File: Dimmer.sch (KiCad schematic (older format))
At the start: 62 parts, among them J1 220to12, J10 Detect_nullA, J11 220v_OUT, J12 Load_cntrlA, J13 ADC, J14 Conn_01x01, J15 Conn_01x01, J16 Conn_01x01, J17 Conn_01x01, J18 Conn_01x01, J19 Conn_01x01, J2 Prog, J22 SPI, J3 UART0, J4 Mode, J5 Load_cntrl, J6 Detect_null, J7 I2C, J8 ADC, J9 220v_IN, Q1 IRFP460APBF, Q2 IRFP460APBF, Q3 BC807, SW1 SW_Push, SW2 SW_Push, U2 ESP32-WROOM-32D, U3 L78L33_SO8, U4 TLP185, k1 Key, k2 Key, k3 Key, k4 Key, k5 Key, k6 Key, k7 Key

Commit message: Add files via upload
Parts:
- removed J10: Detect_nullA, Connector:FanPinHeader_1x03_P2.54mm_Vertical, symbol Connector_Generic:Conn_01x03
- removed J12: Load_cntrlA, Connector:FanPinHeader_1x03_P2.54mm_Vertical, symbol Connector_Generic:Conn_01x03
- removed J16, J17, J18, J19: Conn_01x01, Touch_pad:polz_razjem, symbol Connector_Generic:Conn_01x01
- removed J4: Mode, Connector_PinHeader_2.54mm:PinHeader_1x04_P2.54mm_Vertical_SMD_Pin1Left, symbol Connector_Generic:Conn_01x02
- removed J5: Load_cntrl, Connector:FanPinHeader_1x03_P2.54mm_Vertical, symbol Connector_Generic:Conn_01x03
- removed J6: Detect_null, Connector:FanPinHeader_1x03_P2.54mm_Vertical, symbol Connector_Generic:Conn_01x03
- removed k1: Key, Touch_pad:TestPoint_Pad_2.5x2.5sm, symbol Dimmer-rescue:Key-Touchpad-Dimmer-rescue
- added J10, J12, J5, J6: Pin, SMout:polz_razjem, symbol Connector_Generic:Conn_01x01
- added J16, J4: Conn_01x05, Connector_PinHeader_2.54mm:PinHeader_1x05_P2.54mm_Vertical, symbol Connector_Generic:Conn_01x05
- added J20: Rst, SMout:polz_razjem, symbol Connector_Generic:Conn_01x01
- added J23: Mode, SMout:2pins, symbol Connector_Generic:Conn_01x02
- C1, C8: footprint Capacitor_SMD:C_1210_3225Metric -> Capacitor_SMD:C_0402_1005Metric
- C11, C2: footprint Capacitor_SMD:C_1210_3225Metric -> Capacitor_SMD:C_0805_2012Metric
- J1: footprint Converter_ACDC:Converter_ACDC_MeanWell_IRM-02-xx_THT -> SMout:oblast_bp; symbol Dimmer-rescue:HEADER_2x2-w_connectors-Dimmer-rescue -> Dimmer-rescue:HEADER_2x2-w_connectors-Dimmer-rescue-Dimmer-rescue
- J11, J9: footprint Connector_Phoenix_MC_HighVoltage:PhoenixContact_MC_1,5_2-G-5.08_1x02_P5.08mm_Horizontal -> SMout:OUT_IN(1)
- J13, J8: footprint Touch_pad:polz_razjem -> SMout:polz_razjem
- J14, J15: value Conn_01x01 -> Pin; footprint Touch_pad:polz_razjem -> SMout:polz_razjem
- J2: footprint Connector_PinHeader_2.54mm:PinHeader_1x02_P2.54mm_Vertical_SMD_Pin1Left -> SMout:2pins
- J22: footprint Connector_PinHeader_2.54mm:PinHeader_1x04_P2.54mm_Vertical_SMD_Pin1Right -> Connector_PinHeader_2.54mm:PinHeader_1x03_P2.54mm_Vertical_SMD_Pin1Right
- R10: footprint Resistor_SMD:R_0603_1608Metric -> Resistor_SMD:R_1206_3216Metric
- R13, R2, R9: footprint Resistor_SMD:R_0603_1608Metric -> Resistor_SMD:R_0805_2012Metric
- R7: footprint Resistor_SMD:R_0603_1608Metric -> Resistor_SMD:R_2512_6332Metric
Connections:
- net GPIO26 is gone; now on net cntrl: U2.11 (IO26)
- net +3V3: now also J16.1 (Pin_1), J4.1 (Pin_1)
- net GND: now also J16.5 (Pin_5), J4.5 (Pin_5)
- net Mode: now also J23.1 (Pin_1)
- net cntrl: now also J16.2 (Pin_2); no longer D7.3 (IN+)
- net at R2.2, SW1.2, U2.3 (EN): now also J20.1 (Pin_1)
- net at SW2.2: now also J23.2 (Pin_2)
- net at U2.17 (SHD/SD2): now also J6.1 (Pin_1)
- net at U2.18 (SWP/SD3): now also J10.1 (Pin_1)
- net at U2.19 (SCS/CMD): now also J15.1 (Pin_1)
- net at U2.20 (SCK/CLK): now also J12.1 (Pin_1)
- net at U2.22 (SDI/SD1): now also J5.1 (Pin_1); no longer J15.1 (Pin_1)
- net Detect_null: now reaches U4.6
- net Detect_null: now also J4.4 (Pin_4)
- net at R9.2, TH1.1: now also J4.3 (Pin_3)
- net GPIO17 renamed null
- net null: now also J16.4 (Pin_4)
- net GPIO32 renamed termo_bp
- net termo_bp: now also J16.3 (Pin_3)
- net GPIO35 renamed photo
- new net Load_cntrl: D7.3 (IN+), J4.2 (Pin_2)
- no-connect marks 0 -> 1
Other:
- moved on the sheet: J22, SW2

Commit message: Add files via upload
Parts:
- removed TH1, TH2: Thermistor_NTC, Resistor_SMD:R_1206_3216Metric_Pad1.30x1.75mm_HandSolder, symbol Device:Thermistor_NTC
- added J17: I2C, Connector_PinSocket_2.54mm:PinSocket_1x03_P2.54mm_Horizontal, symbol Connector_Generic:Conn_01x03
- added U1: LM75B, SMout:Diodes_SO-8, symbol Sensor_Temperature:LM75B
- J7: footprint Connector_PinHeader_2.54mm:PinHeader_1x04_P2.54mm_Horizontal -> Connector_PinSocket_2.54mm:PinSocket_1x03_P2.54mm_Horizontal
- R13, R9: footprint Resistor_SMD:R_0805_2012Metric -> Resistor_SMD:R_0603_1608Metric
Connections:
- net +3V3: now also U1.8 (+Vs)
- net GND: now also J17.3 (Pin_3), U1.4 (GND), U1.5 (A2), U1.6 (A1), U1.7 (A0)
- net O.S.: now reaches U2.26 (IO4)
- net O.S.: now also J16.3 (Pin_3)
- net at U2.6 (IO34): no longer R13.2
- net at J4.3 (Pin_3): now also U1.3 (O.S.); no longer R9.2
- net termo_bp: no longer names the net of U2.10 (IO25)
- net termo_bp: no longer J16.3 (Pin_3)
- new net SCL: J17.2 (Pin_2), R13.2, U1.2 (SCL)
- new net SDA: J17.1 (Pin_1), R9.2, U1.1 (SDA)
- no-connect marks 1 -> 2
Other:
- moved on the sheet: C11, C8, J4, U3

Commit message: Add files via upload
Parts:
- C1, C8: footprint Capacitor_SMD:C_0402_1005Metric -> Capacitor_SMD:C_0805_2012Metric
- D5, D6: footprint LED_THT:LED_D3.0mm_Clear -> LED_SMD:LED_0805_2012Metric
- J17: footprint Connector_PinSocket_2.54mm:PinSocket_1x03_P2.54mm_Horizontal -> Connector_PinSocket_2.54mm:PinSocket_1x03_P2.54mm_Vertical
- J22: footprint Connector_PinHeader_2.54mm:PinHeader_1x03_P2.54mm_Vertical_SMD_Pin1Right -> Connector_PinHeader_2.54mm:PinHeader_1x04_P2.54mm_Vertical
- J3: footprint Connector_PinHeader_2.54mm:PinHeader_1x04_P2.54mm_Horizontal -> SMout:4pins
- J7: footprint Connector_PinSocket_2.54mm:PinSocket_1x03_P2.54mm_Horizontal -> Connector_PinHeader_2.54mm:PinHeader_1x03_P2.54mm_Horizontal
- R3: footprint OptoDevice:R_LDR_5.1x4.3mm_P3.4mm_Vertical -> SMout:R_LDR_5.1x4.3mm_P3.4mm_Vertical
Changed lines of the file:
@@
 F 0 "C8" H 5218 4031 50  0000 L CNN
 F 1 "0.1mk" H 5218 3940 50  0000 L CNN
-F 2 "Capacitor_SMD:C_0402_1005Metric" H 5040 3985 50  0001 C CNN
+F 2 "Capacitor_SMD:C_0805_2012Metric" H 5040 3985 50  0001 C CNN
 F 3 "~" H 5040 3985 50  0001 C CNN
 	1    5040 3985
@@
 F 0 "J7" H 9130 4642 50  0000 L CNN
 F 1 "I2C" H 9130 4551 50  0000 L CNN
-F 2 "Connector_PinSocket_2.54mm:PinSocket_1x03_P2.54mm_Horizontal" H 9050 4600 50  0001 C CNN
+F 2 "Connector_PinHeader_2.54mm:PinHeader_1x03_P2.54mm_Horizontal" H 9050 4600 50  0001 C CNN
 F 3 "~" H 9050 4600 50  0001 C CNN
 	1    9050 4600
@@
 $EndComp
 $Comp
-L Connector_Generic:Conn_01x02 J2
-U 1 1 60C48D5A
-P 8800 2750
-F 0 "J2" H 8880 2742 50  0000 L CNN
-F 1 "Prog" H 8880 2651 50  0000 L CNN
-F 2 "SMout:2pins" H 8800 2750 50  0001 C CNN
-F 3 "~" H 8800 2750 50  0001 C CNN
-	1    8800 2750
-	1    0    0    -1
-$EndComp
-$Comp
 L Connector_Generic:Conn_01x04 J3
 U 1 1 60C3C307
@@
 F 0 "J3" H 9280 3292 50  0000 L CNN
 F 1 "UART0" H 9280 3201 50  0000 L CNN
-F 2 "Connector_PinHeader_2.54mm:PinHeader_1x04_P2.54mm_Horizontal" H 9200 3300 50  0001 C CNN
+F 2 "SMout:4pins" H 9200 3300 50  0001 C CNN
 F 3 "~" H 9200 3300 50  0001 C CNN
 	1    9200 3300
@@
 F 0 "C1" H 1928 2996 50  0000 L CNN
 F 1 "0.01mk" H 1928 2905 50  0000 L CNN
-F 2 "Capacitor_SMD:C_0402_1005Metric" H 1750 2950 50  0001 C CNN
+F 2 "Capacitor_SMD:C_0805_2012Metric" H 1750 2950 50  0001 C CNN
 F 3 "~" H 1750 2950 50  0001 C CNN
 	1    1750 2950
@@
 F 0 "R3" H 9370 5946 50  0000 L CNN
 F 1 "GL5528" H 9370 5855 50  0000 L CNN
-F 2 "OptoDevice:R_LDR_5.1x4.3mm_P3.4mm_Vertical" V 9350 5650 50  0001 L CNN
+F 2 "SMout:R_LDR_5.1x4.3mm_P3.4mm_Vertical" V 9350 5650 50  0001 L CNN
 F 3 "~" H 9300 5850 50  0001 C CNN
 	1    9300 5900
@@
 F 0 "D5" V 9889 5432 50  0000 R CNN
 F 1 "BLUE" V 9798 5432 50  0000 R CNN
-F 2 "LED_THT:LED_D3.0mm_Clear" H 9850 5550 50  0001 C CNN
+F 2 "LED_SMD:LED_0805_2012Metric" H 9850 5550 50  0001 C CNN
 F 3 "~" H 9850 5550 50  0001 C CNN
 	1    9850 5550
@@
 F 0 "D6" V 10289 5432 50  0000 R CNN
 F 1 "RED" V 10198 5432 50  0000 R CNN
-F 2 "LED_THT:LED_D3.0mm_Clear" H 10250 5550 50  0001 C CNN
+F 2 "LED_SMD:LED_0805_2012Metric" H 10250 5550 50  0001 C CNN
 F 3 "~" H 10250 5550 50  0001 C CNN
 	1    10250 5550
@@
 F 0 "J22" H 9135 4217 50  0000 L CNN
 F 1 "SPI" H 9135 4126 50  0000 L CNN
-F 2 "Connector_PinHeader_2.54mm:PinHeader_1x03_P2.54mm_Vertical_SMD_Pin1Right" H 9055 4225 50  0001 C CNN
+F 2 "Connector_PinHeader_2.54mm:PinHeader_1x04_P2.54mm_Vertical" H 9055 4225 50  0001 C CNN
 F 3 "~" H 9055 4225 50  0001 C CNN
 	1    9055 4225
@@
 F 0 "J17" H 3010 4862 50  0000 L CNN
 F 1 "I2C" H 3010 4771 50  0000 L CNN
-F 2 "Connector_PinSocket_2.54mm:PinSocket_1x03_P2.54mm_Horizontal" H 2930 4820 50  0001 C CNN
+F 2 "Connector_PinSocket_2.54mm:PinSocket_1x03_P2.54mm_Vertical" H 2930 4820 50  0001 C CNN
 F 3 "~" H 2930 4820 50  0001 C CNN
 	1    2930 4820
@@
 	1    0    0    -1
 $EndComp
+$Comp
+L Connector_Generic:Conn_01x02 J2
+U 1 1 60C48D5A
+P 8800 2750
+F 0 "J2" H 8880 2742 50  0000 L CNN
+F 1 "Prog" H 8880 2651 50  0000 L CNN
+F 2 "SMout:2pins" H 8800 2750 50  0001 C CNN
+F 3 "~" H 8800 2750 50  0001 C CNN
+	1    8800 2750
+	1    0    0    -1
+$EndComp

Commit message: New regulator, buttons
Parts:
- removed J17: I2C, Connector_PinSocket_2.54mm:PinSocket_1x03_P2.54mm_Vertical, symbol Connector_Generic:Conn_01x03
- removed J23: Mode, SMout:2pins, symbol Connector_Generic:Conn_01x02
- removed J7: I2C, Connector_PinHeader_2.54mm:PinHeader_1x03_P2.54mm_Horizontal, symbol Connector_Generic:Conn_01x03
- removed U3: L78L33_SO8, Package_SO:SOIC-8_3.9x4.9mm_P1.27mm, symbol Regulator_Linear:L78L33_SO8
- added U22: AMS1117-3.3, Package_TO_SOT_SMD:SOT-223-3_TabPin2, symbol Regulator_Linear:AMS1117-3.3
- C11: value 0.33mk -> 1uF
- C8: value 0.1mk -> 0.1uF
- J16, J4: value Conn_01x05 -> Conn_01x06; footprint Connector_PinHeader_2.54mm:PinHeader_1x05_P2.54mm_Vertical -> Connector_PinHeader_2.54mm:PinHeader_1x06_P2.54mm_Vertical; symbol Connector_Generic:Conn_01x05 -> Connector_Generic:Conn_01x06
- Mode1: renamed from SW2; footprint Button_Switch_SMD:SW_DIP_SPSTx01_Slide_6.7x4.1mm_W6.73mm_P2.54mm_LowProfile_JPin -> Touch_pad:aLIEXPRESS_BUTTON_G71Y
- RST2: renamed from SW1; footprint Button_Switch_SMD:SW_DIP_SPSTx01_Slide_6.7x4.1mm_W6.73mm_P2.54mm_LowProfile_JPin -> Touch_pad:aLIEXPRESS_BUTTON_G71Y
- renumbered J12 to CLK1, J15 to CMD1, J20 to RST1, J14 to SD0, J5 to SD1, J6 to SD2, J10 to SD3, J13 to S_VN1, J8 to S_VP1
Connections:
- net +12V: now also U22.3 (VI)
- net +3V3: now also U22.2 (VO)
- net Detect_null: now also J4.3 (Pin_3); no longer J4.4 (Pin_4)
- net GND: now also J16.6 (Pin_6), J4.6 (Pin_6), RST2.2, U22.1 (GND); no longer J16.5 (Pin_5), J4.5 (Pin_5), RST2.1
- net Mode: now also Mode1.2
- net SCL: now also J16.4 (Pin_4), J4.4 (Pin_4), U2.36 (IO22)
- net SDA: now also J16.5 (Pin_5), J4.5 (Pin_5), U2.33 (IO21)
- net null: now also J16.3 (Pin_3); no longer J16.4 (Pin_4)
- net at R2.2, RST1.1 (Pin_1), U2.3 (EN): now also RST2.1; no longer RST2.2
- net at U1.3 (O.S.): no longer J4.3 (Pin_3)
- net O.S.: no longer names the net of U2.26 (IO4)
- net O.S.: no longer J16.3 (Pin_3)
- no-connect marks 2 -> 4
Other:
- moved on the sheet: RST2

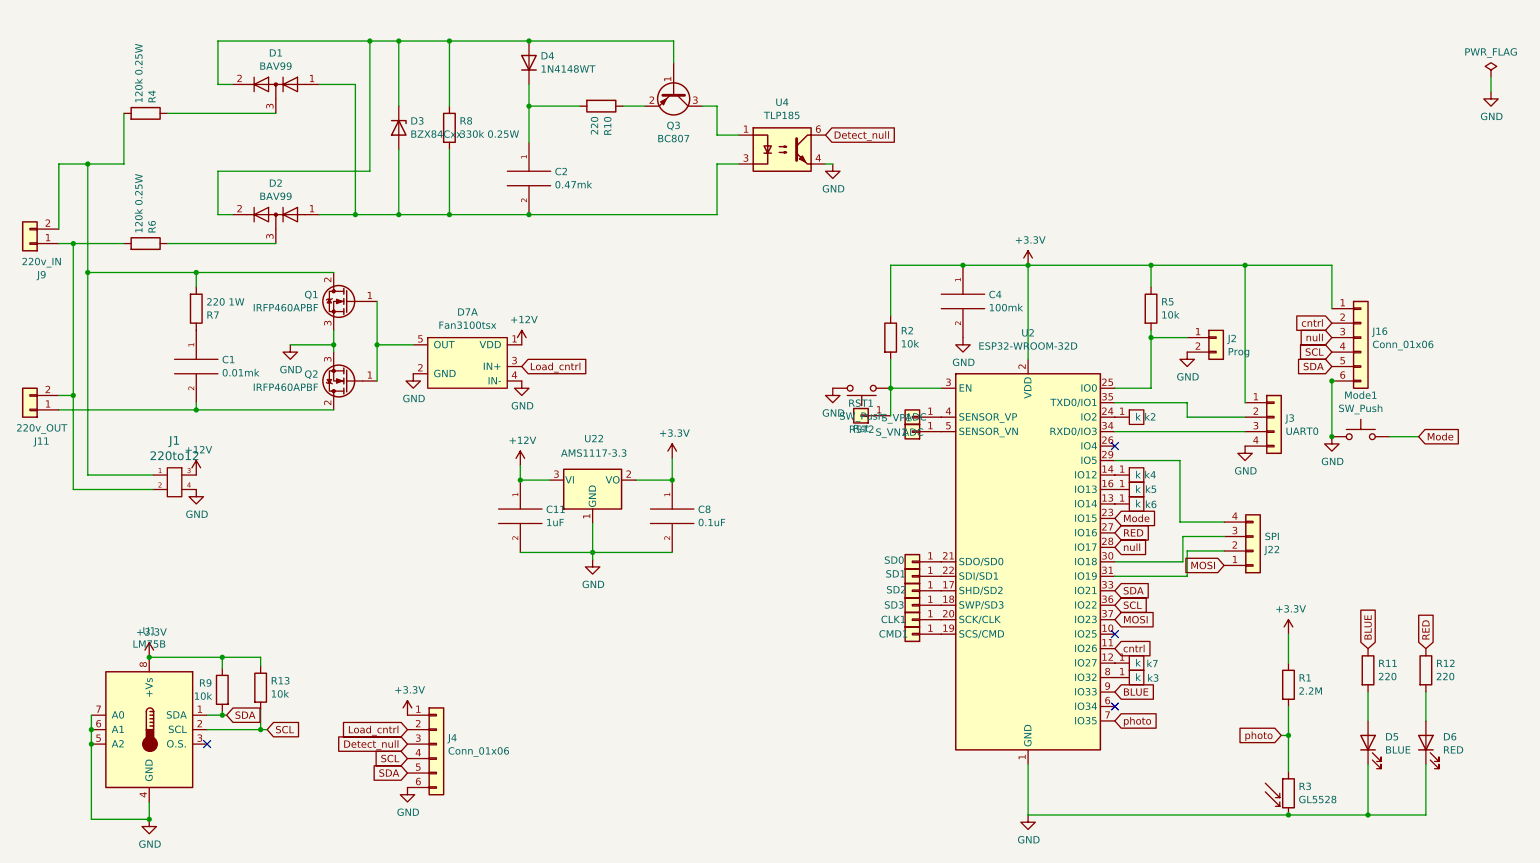
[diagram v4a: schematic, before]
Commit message: Заменены посадочные места, переразведена нижняя плата
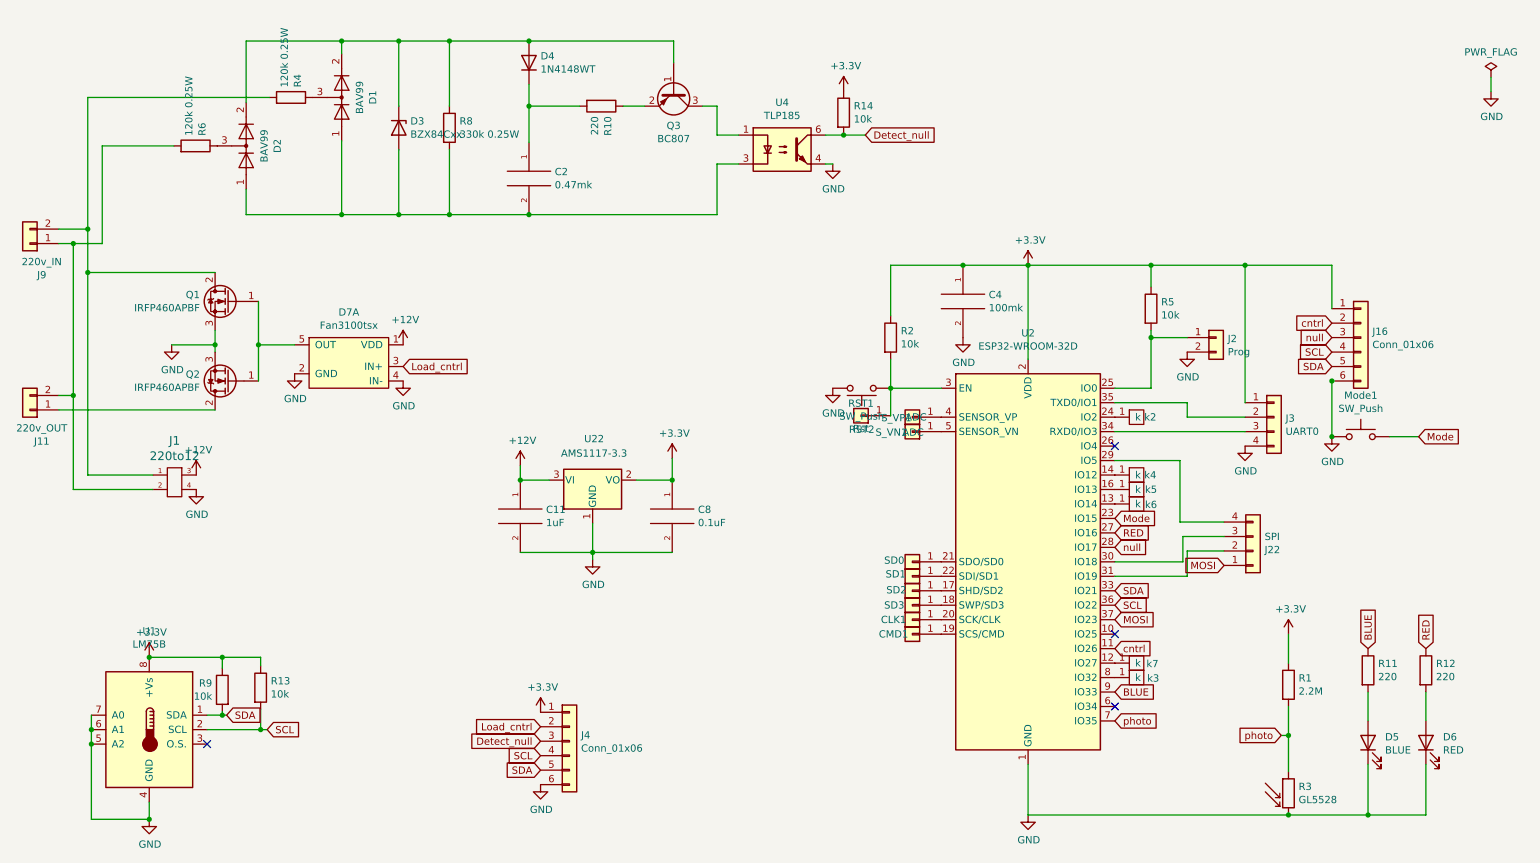
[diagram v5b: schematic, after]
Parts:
- removed C1: 0.01mk, Capacitor_SMD:C_0805_2012Metric, symbol pspice:C
- removed R7: 220 1W, Resistor_SMD:R_2512_6332Metric, symbol Device:R
- added R14: 10k, Resistor_SMD:R_0805_2012Metric, symbol Device:R
- C4: footprint Capacitor_SMD:C_1210_3225Metric -> Capacitor_SMD:C_0805_2012Metric
- D4: footprint Diode_SMD:D_SOD-523 -> Diode_SMD:D_SOD-123
- R1, R10, R11, R12: footprint Resistor_SMD:R_1206_3216Metric -> Resistor_SMD:R_0805_2012Metric
- R13, R4, R5, R6, R8, R9: footprint Resistor_SMD:R_0603_1608Metric -> Resistor_SMD:R_0805_2012Metric
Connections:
- net +3V3: now also R14.1
- net Detect_null: now also R14.2
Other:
- moved on the sheet: D1, D2, D7A, J4, Q1, Q2, R4, R6

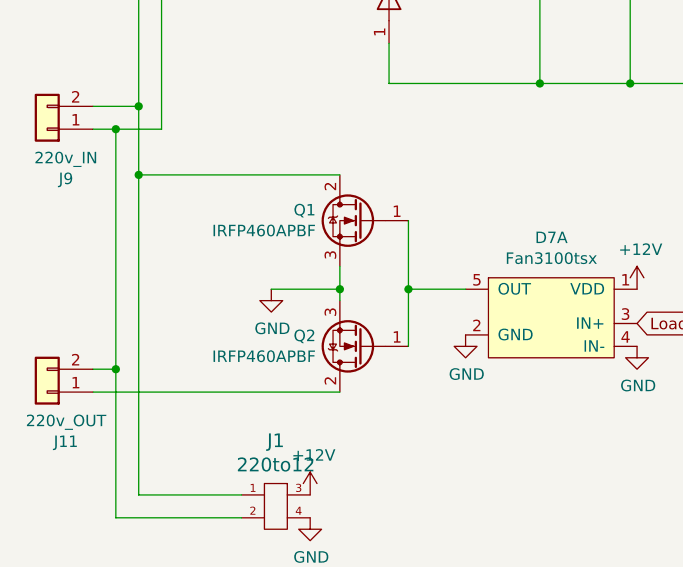
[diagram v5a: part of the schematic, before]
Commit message: Добавлены С1 и R7
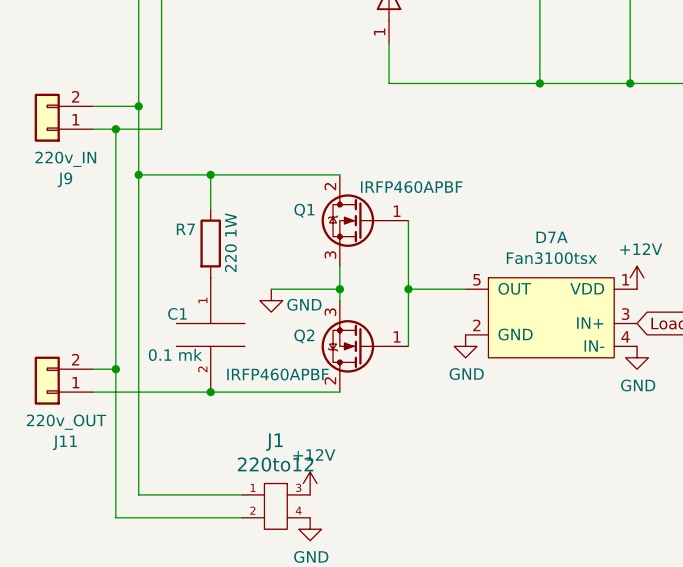
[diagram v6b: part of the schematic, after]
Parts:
- added C1: 0.1 mk, Capacitor_SMD:C_0805_2012Metric, symbol pspice:C
- added R7: 220 1W, Resistor_SMD:R_2512_6332Metric, symbol Device:R
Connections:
- net at J11.1 (Pin_1), Q2.2 (D): now also C1.2
- net at J1.1, J9.2 (Pin_2), Q1.2 (D)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: now also R7.1
- new net: C1.1, R7.2
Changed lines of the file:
@@
 P 1580 2800
 F 0 "#PWR0113" H 1580 2550 50  0001 C CNN
-F 1 "GND" H 1585 2627 50  0000 C CNN
+F 1 "GND" H 1725 2730 50  0000 C CNN
 F 2 "" H 1580 2800 50  0001 C CNN
 F 3 "" H 1580 2800 50  0001 C CNN
@@
 P 1980 3050
 F 0 "Q2" H 2185 3004 50  0000 L CNN
-F 1 "IRFP460APBF" H 2185 3095 50  0000 L CNN
+F 1 "IRFP460APBF" H 2125 3175 50  0000 L CNN
 F 2 "Package_TO_SOT_THT:TO-247-3_Horizontal_TabDown" H 1980 3050 50  0001 C CIN
 F 3 "https://www.wolfspeed.com/media/downloads/825/C3M0280090D.pdf" H 1980 3050 50  0001 L CNN
@@
 P 1980 2500
 F 0 "Q1" H 2185 2546 50  0000 L CNN
-F 1 "IRFP460APBF" H 2185 2455 50  0000 L CNN
+F 1 "IRFP460APBF" H 1540 2645 50  0000 L CNN
 F 2 "Package_TO_SOT_THT:TO-247-3_Horizontal_TabDown" H 1980 2500 50  0001 C CIN
 F 3 "https://www.wolfspeed.com/media/downloads/825/C3M0280090D.pdf" H 1980 2500 50  0001 L CNN
@@
 	1    0    0    -1
 $EndComp
+$Comp
+L pspice:C C1
+U 1 1 6168A513
+P 1315 3000
+F 0 "C1" H 1125 3090 50  0000 L CNN
+F 1 "0.1 mk" H 1040 2910 50  0000 L CNN
+F 2 "Capacitor_SMD:C_0805_2012Metric" H 1315 3000 50  0001 C CNN
+F 3 "~" H 1315 3000 50  0001 C CNN
+	1    1315 3000
+	1    0    0    -1
+$EndComp
+$Comp
+L Device:R R7
+U 1 1 6168FD9E
+P 1315 2600
+F 0 "R7" H 1160 2660 50  0000 L CNN
+F 1 "220 1W" V 1405 2470 50  0000 L CNN
+F 2 "Resistor_SMD:R_2512_6332Metric" V 1245 2600 50  0001 C CNN
+F 3 "~" H 1315 2600 50  0001 C CNN
+	1    1315 2600
+	1    0    0    -1
+$EndComp
 Wire Wire Line
-	800  3250 1880 3250
+	1000 2300 1315 2300
 Wire Wire Line
-	1000 2300 1880 2300
+	1315 2450 1315 2300
+Connection ~ 1315 2300
+Wire Wire Line
+	1315 2300 1880 2300
+Wire Wire Line
+	800  3250 1315 3250
+Connection ~ 1315 3250
+Wire Wire Line
+	1315 3250 1880 3250
 $EndSCHEMATC
